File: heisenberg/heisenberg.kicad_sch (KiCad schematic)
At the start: 5 parts, among them J1 HLE-110-02-L-DV-BE-K-TR, J2 HLE-110-02-L-DV-BE-K-TR, J3 TSM-108-01-F-DV, J4 S16B-XH-A, U1 Teensy4.1

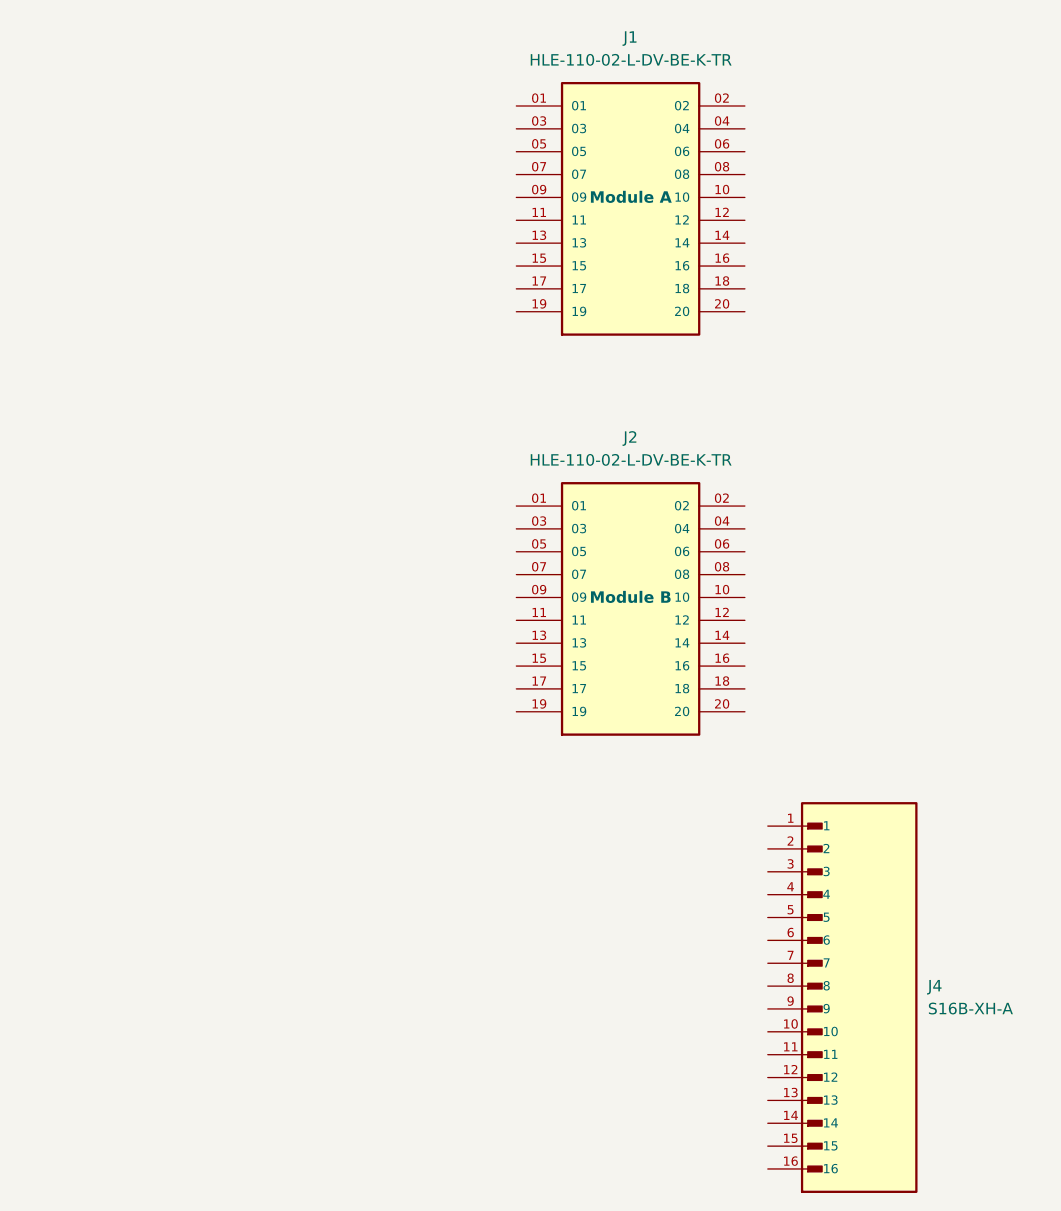
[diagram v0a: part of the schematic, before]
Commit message: Created Tuco board outline, heisenberg pin labels
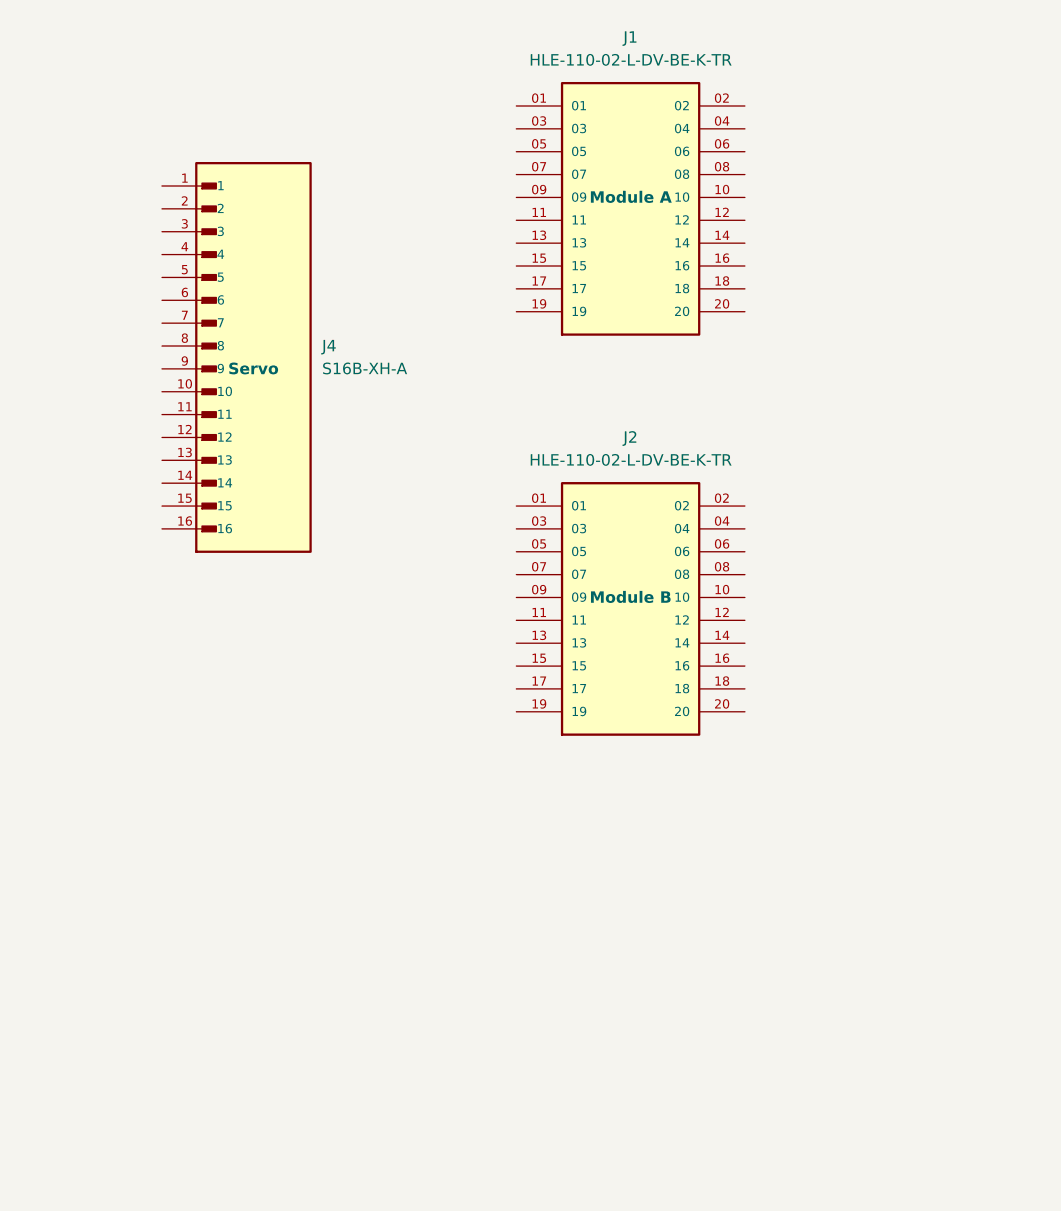
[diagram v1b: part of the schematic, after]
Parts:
- J4: Label (none) -> Servo
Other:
- moved on the sheet: J4
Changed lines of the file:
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@@
 	(symbol
 		(lib_id "MDFC Common:S16B-XH-A")
-		(at 260.35 125.73 0)
+		(at 193.04 54.61 0)
 		(unit 1)
 		(body_style 1)
@@
 		(fields_autoplaced yes)
 		(property "Reference" "J4"
-			(at 267.97 123.1899 0)
+			(at 200.66 52.0699 0)
 			(show_name no)
 			(do_not_autoplace no)
@@
 		)
 		(property "Value" "S16B-XH-A"
-			(at 267.97 125.7299 0)
+			(at 200.66 54.6099 0)
 			(show_name no)
 			(do_not_autoplace no)
@@
 		)
 		(property "Footprint" "Connector_JST:JST_XH_S16B-XH-A_1x16_P2.50mm_Horizontal"
-			(at 260.35 125.73 0)
+			(at 193.04 54.61 0)
 			(hide yes)
 			(show_name no)
@@
 		)
 		(property "Datasheet" ""
-			(at 260.35 125.73 0)
+			(at 193.04 54.61 0)
 			(hide yes)
 			(show_name no)
@@
 		)
 		(property "Description" "Connector Header Through Hole, Right Angle 16 position 0.098 (2.50mm)"
-			(at 260.35 125.73 0)
+			(at 193.04 54.61 0)
 			(hide yes)
 			(show_name no)
@@
 		)
 		(property "MF" "JST Sales America Inc."
-			(at 260.35 125.73 0)
+			(at 193.04 54.61 0)
 			(hide yes)
 			(show_name no)
@@
 		)
 		(property "Package" "None"
-			(at 260.35 125.73 0)
+			(at 193.04 54.61 0)
 			(hide yes)
 			(show_name no)
@@
 		)
 		(property "Price" "None"
-			(at 260.35 125.73 0)
+			(at 193.04 54.61 0)
 			(hide yes)
 			(show_name no)
@@
 		)
 		(property "Check_prices" "https://www.snapeda.com/parts/S16B-XH-A/JST/view-part/?ref=eda"
-			(at 260.35 125.73 0)
+			(at 193.04 54.61 0)
 			(hide yes)
 			(show_name no)
@@
 		)
 		(property "SnapEDA_Link" "https://www.snapeda.com/parts/S16B-XH-A/JST/view-part/?ref=snap"
-			(at 260.35 125.73 0)
+			(at 193.04 54.61 0)
 			(hide yes)
 			(show_name no)
@@
 		)
 		(property "MP" "S16B-XH-A"
-			(at 260.35 125.73 0)
+			(at 193.04 54.61 0)
 			(hide yes)
 			(show_name no)
@@
 		)
 		(property "Availability" "In Stock"
-			(at 260.35 125.73 0)
+			(at 193.04 54.61 0)
 			(hide yes)
 			(show_name no)
@@
 		)
 		(property "MANUFACTURER" "JST"
-			(at 260.35 125.73 0)
+			(at 193.04 54.61 0)
 			(hide yes)
 			(show_name no)
@@
 			)
 		)
+		(property "Label" "Servo"
+			(at 193.04 54.61 0)
+			(show_name no)
+			(do_not_autoplace no)
+			(effects
+				(font
+					(size 1.27 1.27)
+					(thickness 0.254)
+					(bold yes)
+				)
+			)
+		)

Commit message: Main board MOD A&B pins & routing
V1 of  the initial module A & B routing so other people can have a starting point for their pin layout

dont mind the naming scheme i need to fix that
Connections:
- net +5V: now reaches J1.01
- net +5V: now also J2.19, J3.3, J3.4, J4.16
- net GND: now reaches J1.02
- net GND: now also J1.04, J1.05, J1.07, J2.13, J2.15, J2.18, J2.20, J3.1, J3.11, J3.13, J3.15, J3.2, J4.1, J4.3, J4.5
- net +24V: now reaches J1.03
- net +24V: now also J2.17, J3.10
- net PWM_CS_A: now reaches J1.06
- net PWM_CS_A: now also U1.28 (36_CS)
- net SPI_A_CS: now reaches J1.08
- net SPI_A_CS: now also U1.29 (37_CS)
- net UART_A_TX7: now reaches J1.09
- net UART_A_TX7: now also U1.21 (29_TX7)
- net A14_A: now reaches J1.10
- net A14_A: now also U1.30 (38_CS1_IN1)
- net UART_A_RX7: now reaches J1.11
- net UART_A_RX7: now also U1.20 (28_RX7)
- net SPI_A_SCK: now reaches J1.12
- net SPI_A_SCK: now also U1.35 (13_SCK_LED)
- net SPI_A_MISO: now reaches J1.13
- net SPI_A_MISO: now also U1.14 (12_MISO_MQSL)
- net A0_TX: now reaches J1.14
- net A0_TX: now also U1.36 (14_A0_TX3_SPDIF_OUT)
- net SPI_A_MOSI: now reaches J1.15
- net SPI_A_MOSI: now also U1.13 (11_MOSI_CTX1)
- net I2C_A_SCL: now reaches J1.16
- net I2C_A_SCL: now also U1.41 (19_A5_SCL)
- net PWM_A: now reaches J1.17
- net PWM_A: now also U1.11 (9_OUT1C)
- net I2C_A_SDA: now reaches J1.18
- net I2C_A_SDA: now also U1.40 (18_A4_SDA)
- net A15_A: now reaches J1.19
- net A15_A: now also U1.31 (39_MISO1_OUT1A)
- net A1_RX: now reaches J1.20
- net A1_RX: now also U1.37 (15_A1_RX3_SPDIF_IN)
- net A17_B: now reaches J2.01
- net A17_B: now also U1.33 (41_A17)
- net I2C_B_SCL: now reaches J2.02
- net I2C_B_SCL: now also U1.38 (16_A2_RX4_SCL1)
- net SPI_B_CS1: now reaches J2.03
- net SPI_B_CS1: now also U1.2 (0_RX1_CRX2_CS1)
- net I2C_B_SDA: now reaches J2.04
- net I2C_B_SDA: now also U1.39 (17_A3_TX4_SDA1)
- net SPI_B_MISO1: now reaches J2.05
- net SPI_B_MISO1: now also U1.3 (1_TX1_CTX2_MISO1)
- net A7_RX5: now reaches J2.06
- net A7_RX5: now also U1.43 (21_A7_RX5_BCLK1)
- net PWM1_B: now reaches J2.07
- net PWM1_B: now also U1.12 (10_CS_MQSR)
- net A6_TX5: now reaches J2.08
- net A6_TX5: now also U1.42 (20_A6_TX5_LRCLK1)
- net SPI_B_MOSI1: now reaches J2.09
- net SPI_B_MOSI1: now also U1.18 (26_A12_MOSI1)
- net A16_B: now reaches J2.10
- net A16_B: now also U1.32 (40_A16)
- net SPI_B_SCK1: now reaches J2.11
- net SPI_B_SCK1: now also U1.19 (27_A13_SCK1)
- net TX8: now reaches J2.12
- net TX8: now also U1.27 (35_TX8)
- net RX8: now reaches J2.14
- net RX8: now also U1.26 (34_RX8)
- net PWM_B: now reaches J2.16
- net PWM_B: now also U1.25 (33_MCLK2)
- net V_servo: now reaches J3.12
- net V_servo: now also J3.14, J3.16, J4.2, J4.4, J4.6
- net GPIO_PWR: now reaches J3.5
- net GPIO_PWR: now also U1.24 (32_OUT1B)
- net A_RX6_SDA2_PWM: now reaches J3.6
- net A_RX6_SDA2_PWM: now also U1.17 (25_A11_RX6_SDA2)
- net A_CTX1_PWM: now reaches J3.7
- net A_CTX1_PWM: now also U1.44 (22_A8_CTX1)
- net A_TX6_SCL2_PWM: now reaches J3.8
- net A_TX6_SCL2_PWM: now also U1.16 (24_A10_TX6_SCL2)
- net A_CRX1_PWM: now reaches J3.9
- net A_CRX1_PWM: now also U1.45 (23_A9_CRX1_MCLK1)
- net PWM_TX2: now reaches J4.10
- net PWM_TX2: now also U1.9 (7_RX2_OUT1A)
- net PWM_5: now reaches J4.11
- net PWM_5: now also U1.8 (6_OUT1D)
- net PWM_4: now reaches J4.12
- net PWM_4: now also U1.7 (5_IN2)
- net PWM_3: now reaches J4.13
- net PWM_3: now also U1.6 (4_BCLK2)
- net PWM_2: now reaches J4.14
- net PWM_2: now also U1.5 (3_LRCLK2)
- net PWM_1: now reaches J4.15
- net PWM_1: now also U1.4 (2_OUT2)
- net CAN_Servo_CTX3: now reaches J4.7
- net CAN_Servo_CTX3: now also U1.23 (31_CTX3)
- net CAN_Servo_CRX3: now reaches J4.8
- net CAN_Servo_CRX3: now also U1.22 (30_CRX3)
- net PWM_RX2: now reaches J4.9
- net PWM_RX2: now also U1.10 (8_TX2_IN1)
- no-connect marks 0 -> 25
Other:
- note added: "outer side of tthe connector"
- note added: "this side is the outter side of the tensy in layout all correlating pins here need to have their connecter on the outter side"
- moved on the sheet: J1, J2, J3, J4

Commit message: attempt number 2 at routing
This time they are identical schematic layout for A & B and i used the 4 layers to route to potential via points b4 connection
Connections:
- net +24V: now also J1.05, J2.05; no longer J1.03, J2.17
- net +5V: now also J1.07, J2.07; no longer J1.01, J2.19
- net A0_TX: now also J1.12; no longer J1.14
- net A14_A: now also J1.14; no longer J1.10
- net A15_A: now also J1.09; no longer J1.19
- net A16_B: now also J2.14; no longer J2.10
- net A17_B: now also J2.09; no longer J2.01
- net A1_RX: now also J1.10; no longer J1.20
- net A6_TX5: now also J2.12; no longer J2.08
- net A7_RX5: now also J2.10; no longer J2.06
- net GND: now also J1.01, J1.03, J2.01, J2.02, J2.03, J2.04; no longer J1.05, J1.07, J2.13, J2.15, J2.18, J2.20
- net I2C_A_SCL: now also J1.06; no longer J1.16
- net I2C_A_SDA: now also J1.08; no longer J1.18
- net I2C_B_SCL: now also J2.06; no longer J2.02
- net I2C_B_SDA: now also J2.08; no longer J2.04
- net PWM1_B: no longer J2.07
- net PWM_A: now also J1.15; no longer J1.17
- net PWM_B: now also J2.15; no longer J2.16
- net PWM_CS_A: now also J1.20; no longer J1.06
- net SPI_A_CS: now also J1.11; no longer J1.08
- net SPI_A_MOSI: now also J1.17; no longer J1.15
- net SPI_A_SCK: now also J1.19; no longer J1.12
- net SPI_B_CS1: now also J2.11; no longer J2.03
- net SPI_B_MISO1: now also J2.13; no longer J2.05
- net SPI_B_MOSI1: now also J2.17; no longer J2.09
- net SPI_B_SCK1: now also J2.19; no longer J2.11
- net UART_A_RX7: now also J1.18; no longer J1.11
- net UART_A_TX7: now also J1.16; no longer J1.09
- net RX8 renamed UART_B_RX8
- net UART_B_RX8: now also J2.18; no longer J2.14
- net TX8 renamed UART_B_TX8
- net UART_B_TX8: now also J2.16; no longer J2.12
- new net PWM_CS_B: J2.20

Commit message: Update heisenberg.kicad_sch
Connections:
- net PWM_CS_B is gone; now on net PWM1_B: J2.20
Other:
- note added: "text test 5"
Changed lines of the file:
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@@
+		)
+	)
+	(text "text test\n5"
+		(exclude_from_sim no)
+		(at 209.296 149.098 0)
+		(effects
+			(font
+				(size 1.27 1.27)
+			)
 		)
 	)
@@
 		)
 	)
-	(label "PWM_CS_B"
+	(label "PWM1_B"
 		(at 259.588 104.902 180)
 		(effects

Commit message: V2 pin layout main board
Rerouted the wiring to the conectors on the main board in a better less cluttered way all that it needs is vias b4 connecting
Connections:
- net A15_A: now also J1.20; no longer J1.09
- net A17_B: now also J2.20; no longer J2.09
- net PWM1_B: now also J2.09; no longer J2.20
- net PWM_CS_A: now also J1.09; no longer J1.20
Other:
- note removed: "outer side of tthe connector"
- note removed: "this side is the outter side of the tensy in layout all correlating pins here need to have their connecter on the outter side"
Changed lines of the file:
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@@
 	(generator_version "10.0")
 	(paper "A4")
-	(text "outer side of tthe connector\n"
-		(exclude_from_sim no)
-		(at 250.952 26.162 0)
-		(effects
-			(font
-				(size 1.27 1.27)
-			)
-		)
-	)
 	(text "text test\n5"
 		(exclude_from_sim no)
 		(at 209.296 149.098 0)
-		(effects
-			(font
-				(size 1.27 1.27)
-			)
-		)
-	)
-	(text "this side is the outter side of the tensy in layout\n\nall correlating pins here need to have their connecter on the outter side\n"
-		(exclude_from_sim no)
-		(at 166.37 17.018 0)
 		(effects
 			(font
@@
 	(wire
 		(pts
-			(xy 220.472 55.372) (xy 232.918 55.372)
+			(xy 220.472 55.372) (xy 230.886 55.372)
 		)
 		(stroke
@@
 	(wire
 		(pts
-			(xy 189.738 42.672) (xy 195.072 42.672)
+			(xy 185.166 42.672) (xy 195.072 42.672)
 		)
 		(stroke
@@
 		)
 	)
+	(label "PWM1_B"
+		(at 205.994 92.202 0)
+		(effects
+			(font
+				(size 1.27 1.27)
+			)
+			(justify left bottom)
+		)
+	)
 	(label "UART_B_TX8"
 		(at 263.906 99.822 180)
@@
 		)
 	)
-	(label "PWM_CS_A"
-		(at 232.918 55.372 180)
+	(label "A15_A"
+		(at 230.886 55.372 180)
 		(effects
 			(font
@@
 		)
 	)
+	(label "PWM_CS_A"
+		(at 185.166 42.672 0)
+		(effects
+			(font
+				(size 1.27 1.27)
+			)
+			(justify left bottom)
+		)
+	)
 	(label "SPI_B_MISO1"
 		(at 212.09 97.282 0)
@@
 		)
 	)
+	(label "A17_B"
+		(at 259.588 104.902 180)
+		(effects
+			(font
+				(size 1.27 1.27)
+			)
+			(justify right bottom)
+		)
+	)
 	(label "GPIO_PWR"
 		(at 47.752 34.798 180)
@@
 		)
 	)
-	(label "PWM1_B"
-		(at 259.588 104.902 180)
-		(effects
-			(font
-				(size 1.27 1.27)
-			)
-			(justify right bottom)
-		)
-	)
 	(label "A16_B"
 		(at 264.414 97.282 180)
@@
 		)
 	)
-	(label "A17_B"
-		(at 205.994 92.202 0)
-		(effects
-			(font
-				(size 1.27 1.27)
-			)
-			(justify left bottom)
-		)
-	)
 	(label "A15_A"
 		(at 156.464 71.12 180)
@@
 		)
 	)
-	(label "A15_A"
-		(at 189.738 42.672 0)
-		(effects
-			(font
-				(size 1.27 1.27)
-			)
-			(justify left bottom)
-		)
-	)

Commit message: updated power pins layouot
apparently this was never pusheded
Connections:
- net +24V: now also J3.8; no longer J3.10
- net +5V: now also J3.10, J3.7; no longer J3.3, J3.4
- net A_CRX1_PWM: now also J3.5; no longer J3.9
- net A_CTX1_PWM: now also J3.3; no longer J3.7
- net A_RX6_SDA2_PWM: now also J3.2; no longer J3.6
- net A_TX6_SCL2_PWM: now also J3.4; no longer J3.8
- net GND: now also J3.6, J3.9; no longer J3.1, J3.2
- net GPIO_PWR renamed GPIO_PMOD
- net GPIO_PMOD: now also J3.1; no longer J3.5
- net PWM_1 renamed PWM_Servo_1
- net PWM_2 renamed PWM_Servo_2
- net PWM_3 renamed PWM_Servo_3
- net PWM_4 renamed PWM_Servo_4
- net PWM_5 renamed PWM_Servo_5
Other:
- note removed: "text test 5"
